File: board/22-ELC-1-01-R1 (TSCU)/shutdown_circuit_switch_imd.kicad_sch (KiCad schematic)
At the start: 9 parts

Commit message: Ready for review
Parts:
- renumbered C1 to C12, D2 to D6, D3 to D7, D4 to D8, D5 to D9, F2 to F1, R1 to R28, R2 to R29, R3 to R30
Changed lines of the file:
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@@
   (symbol (lib_id "Device:R") (at 72.39 137.16 270) (unit 1)
     (in_bom yes) (on_board yes)
-    (property "Reference" "R2" (id 0) (at 72.39 134.62 90))
+    (property "Reference" "R29" (id 0) (at 72.39 134.62 90))
     (property "Value" "10k" (id 1) (at 72.39 137.16 90))
     (property "Footprint" "Resistor_SMD:R_0603_1608Metric_Pad0.98x0.95mm_HandSolder" (id 2) (at 72.39 135.382 90)
@@
   (symbol (lib_id "Device:R") (at 66.04 142.24 180) (unit 1)
     (in_bom yes) (on_board yes)
-    (property "Reference" "R1" (id 0) (at 68.58 142.24 90))
+    (property "Reference" "R28" (id 0) (at 68.58 142.24 90))
     (property "Value" "2.2k" (id 1) (at 66.04 142.24 90))
     (property "Footprint" "Resistor_SMD:R_0603_1608Metric_Pad0.98x0.95mm_HandSolder" (id 2) (at 67.818 142.24 90)
@@
   (symbol (lib_id "power:GND") (at 66.04 146.05 0) (unit 1)
     (in_bom yes) (on_board yes)
-    (property "Reference" "#PWR012" (id 0) (at 66.04 152.4 0)
+    (property "Reference" "#PWR059" (id 0) (at 66.04 152.4 0)
       (effects (font (size 1.27 1.27)) hide)
     )
@@
   (symbol (lib_id "power:GND") (at 90.17 144.78 0) (unit 1)
     (in_bom yes) (on_board yes)
-    (property "Reference" "#PWR016" (id 0) (at 90.17 151.13 0)
+    (property "Reference" "#PWR063" (id 0) (at 90.17 151.13 0)
       (effects (font (size 1.27 1.27)) hide)
     )
@@
   (symbol (lib_id "Device:C_Small") (at 80.01 140.97 180) (unit 1)
     (in_bom yes) (on_board yes)
-    (property "Reference" "C1" (id 0) (at 74.1934 140.97 90))
+    (property "Reference" "C12" (id 0) (at 74.1934 140.97 90))
     (property "Value" "0.1uf" (id 1) (at 76.5048 140.97 90))
     (property "Footprint" "Capacitor_SMD:C_0603_1608Metric_Pad1.08x0.95mm_HandSolder" (id 2) (at 80.01 140.97 0)
@@
   (symbol (lib_id "power:GND") (at 80.01 144.78 0) (unit 1)
     (in_bom yes) (on_board yes)
-    (property "Reference" "#PWR014" (id 0) (at 80.01 151.13 0)
+    (property "Reference" "#PWR061" (id 0) (at 80.01 151.13 0)
       (effects (font (size 1.27 1.27)) hide)
     )
@@
   (symbol (lib_id "Device:R") (at 179.07 144.78 270) (unit 1)
     (in_bom yes) (on_board yes)
-    (property "Reference" "R3" (id 0) (at 179.07 142.24 90))
+    (property "Reference" "R30" (id 0) (at 179.07 142.24 90))
     (property "Value" "1k" (id 1) (at 179.07 144.78 90))
     (property "Footprint" "Resistor_SMD:R_0603_1608Metric_Pad0.98x0.95mm_HandSolder" (id 2) (at 179.07 143.002 90)
@@
   (symbol (lib_id "power:GND") (at 191.77 152.4 0) (unit 1)
     (in_bom yes) (on_board yes)
-    (property "Reference" "#PWR018" (id 0) (at 191.77 158.75 0)
+    (property "Reference" "#PWR065" (id 0) (at 191.77 158.75 0)
       (effects (font (size 1.27 1.27)) hide)
     )
@@
   (symbol (lib_id "Device:Fuse") (at 67.31 82.55 270) (unit 1)
     (in_bom yes) (on_board yes)
-    (property "Reference" "F2" (id 0) (at 67.31 76.2 90))
+    (property "Reference" "F1" (id 0) (at 67.31 76.2 90))
     (property "Value" "2A" (id 1) (at 67.31 78.74 90))
     (property "Footprint" "Fuse:Fuse_1206_3216Metric_Pad1.42x1.75mm_HandSolder" (id 2) (at 67.31 80.772 90)
@@
   (symbol (lib_id "power:+12V") (at 73.66 81.28 0) (unit 1)
     (in_bom yes) (on_board yes)
-    (property "Reference" "#PWR013" (id 0) (at 73.66 85.09 0)
+    (property "Reference" "#PWR060" (id 0) (at 73.66 85.09 0)
       (effects (font (size 1.27 1.27)) hide)
     )
@@
   (symbol (lib_id "power:+5V") (at 90.17 129.54 0) (unit 1)
     (in_bom yes) (on_board yes)
-    (property "Reference" "#PWR015" (id 0) (at 90.17 133.35 0)
+    (property "Reference" "#PWR062" (id 0) (at 90.17 133.35 0)
       (effects (font (size 1.27 1.27)) hide)
     )
@@
   (symbol (lib_id "power:+5V") (at 191.77 137.16 0) (unit 1)
     (in_bom yes) (on_board yes)
-    (property "Reference" "#PWR017" (id 0) (at 191.77 140.97 0)
+    (property "Reference" "#PWR064" (id 0) (at 191.77 140.97 0)
       (effects (font (size 1.27 1.27)) hide)
     )
@@
   (symbol (lib_id "Device:D_Schottky") (at 191.77 148.59 270) (unit 1)
     (in_bom yes) (on_board yes)
-    (property "Reference" "D5" (id 0) (at 193.802 147.4216 90)
+    (property "Reference" "D9" (id 0) (at 193.802 147.4216 90)
       (effects (font (size 1.27 1.27)) (justify left))
     )
@@
   (symbol (lib_id "Device:D_Schottky") (at 191.77 140.97 270) (unit 1)
     (in_bom yes) (on_board yes)
-    (property "Reference" "D4" (id 0) (at 193.802 139.8016 90)
+    (property "Reference" "D8" (id 0) (at 193.802 139.8016 90)
       (effects (font (size 1.27 1.27)) (justify left))
     )
@@
   (symbol (lib_id "Device:D_Schottky") (at 90.17 140.97 270) (unit 1)
     (in_bom yes) (on_board yes)
-    (property "Reference" "D3" (id 0) (at 92.202 139.8016 90)
+    (property "Reference" "D7" (id 0) (at 92.202 139.8016 90)
       (effects (font (size 1.27 1.27)) (justify left))
     )
@@
   (symbol (lib_id "Device:D_Schottky") (at 90.17 133.35 270) (unit 1)
     (in_bom yes) (on_board yes)
-    (property "Reference" "D2" (id 0) (at 92.202 132.1816 90)
-      (effects (font (size 1.27 1.27)) (justify left))
-    )
+    (property "Reference" "D6" (id 0) (at 92.202 132.1816 90)
+      (effects (font (size 1.27 1.27)) (justify left))
+    )

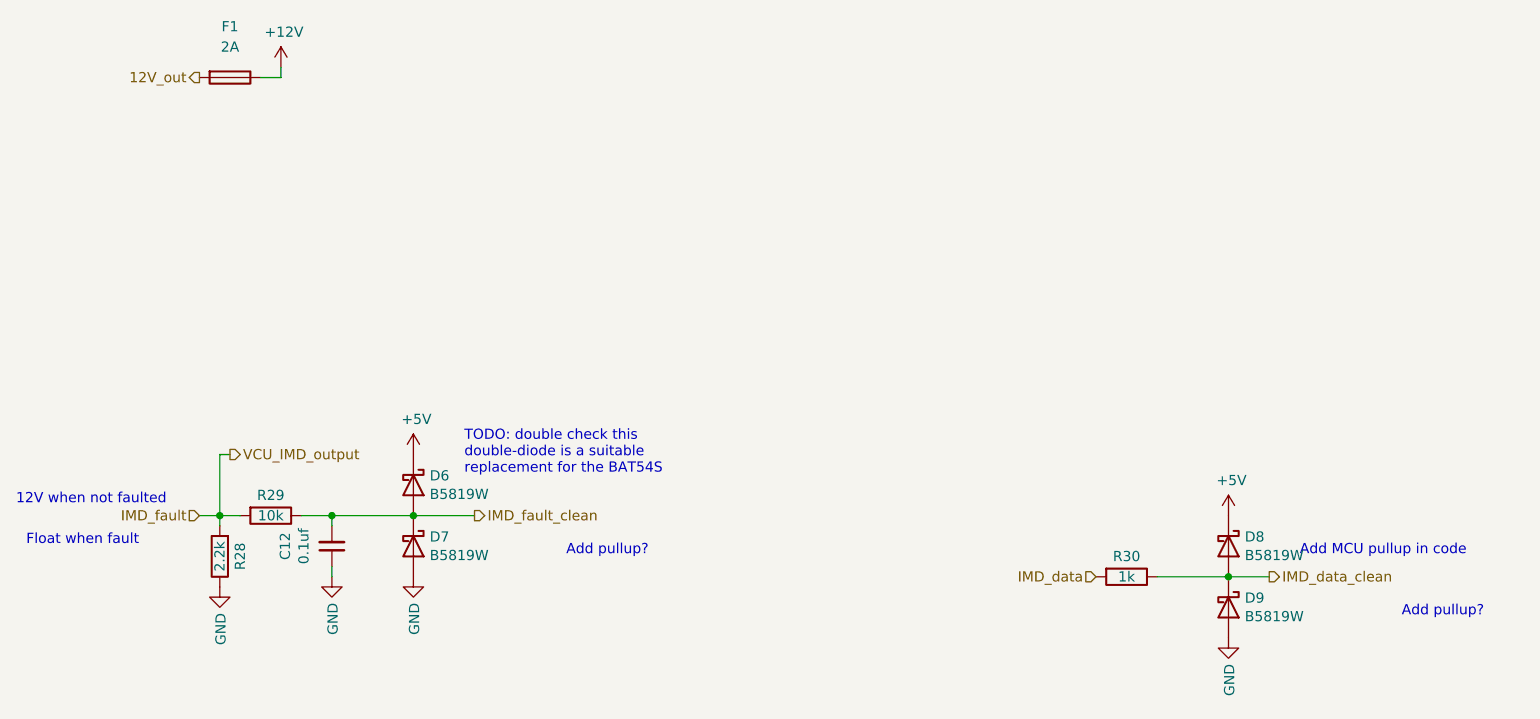
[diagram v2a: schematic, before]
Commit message: All good except need to switch everything to accepting 24v power
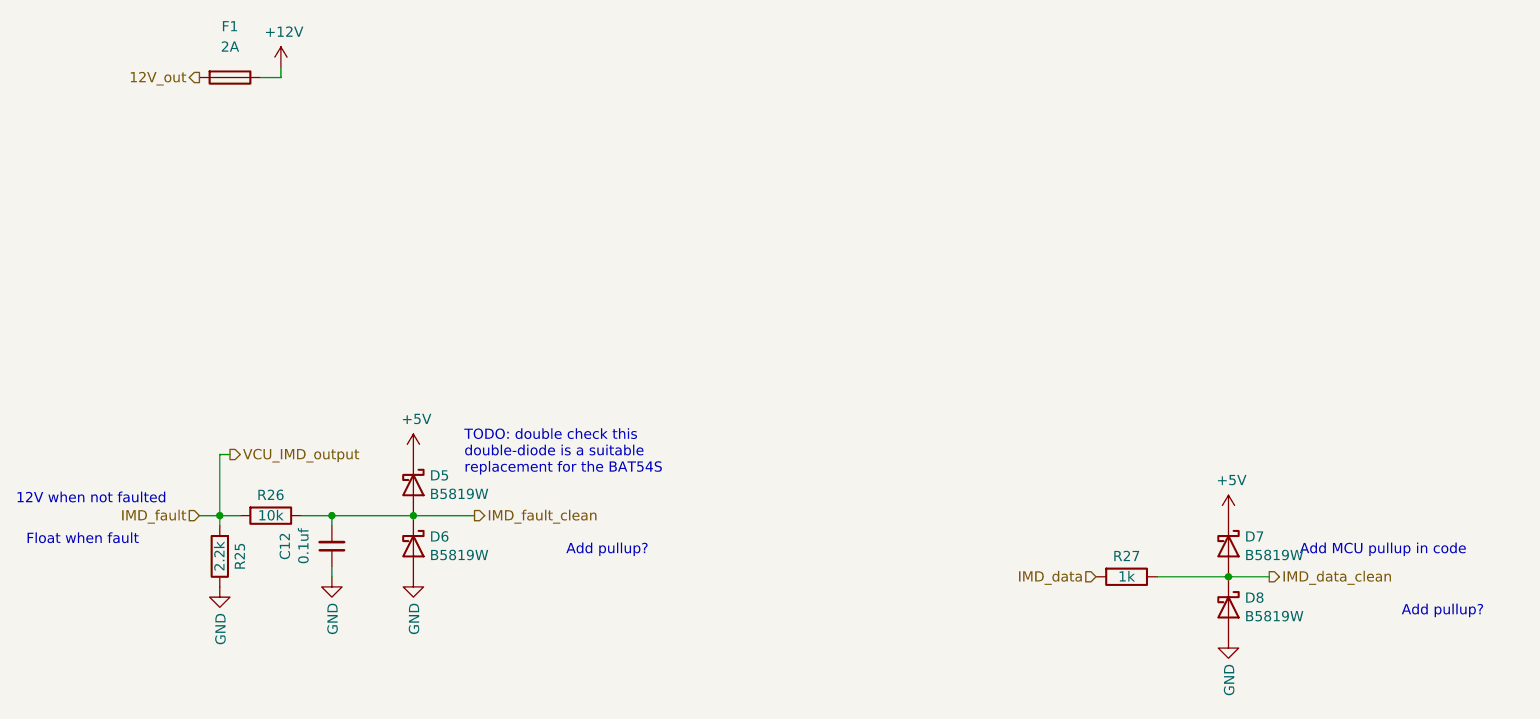
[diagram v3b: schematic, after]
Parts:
- renumbered D6 to D5, D7 to D6, D8 to D7, D9 to D8, R28 to R25, R29 to R26, R30 to R27
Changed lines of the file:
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@@
   (symbol (lib_id "Device:R") (at 72.39 137.16 270) (unit 1)
     (in_bom yes) (on_board yes)
-    (property "Reference" "R29" (id 0) (at 72.39 134.62 90))
+    (property "Reference" "R26" (id 0) (at 72.39 134.62 90))
     (property "Value" "10k" (id 1) (at 72.39 137.16 90))
     (property "Footprint" "Resistor_SMD:R_0603_1608Metric_Pad0.98x0.95mm_HandSolder" (id 2) (at 72.39 135.382 90)
@@
   (symbol (lib_id "Device:R") (at 66.04 142.24 180) (unit 1)
     (in_bom yes) (on_board yes)
-    (property "Reference" "R28" (id 0) (at 68.58 142.24 90))
+    (property "Reference" "R25" (id 0) (at 68.58 142.24 90))
     (property "Value" "2.2k" (id 1) (at 66.04 142.24 90))
     (property "Footprint" "Resistor_SMD:R_0603_1608Metric_Pad0.98x0.95mm_HandSolder" (id 2) (at 67.818 142.24 90)
@@
   (symbol (lib_id "Device:R") (at 179.07 144.78 270) (unit 1)
     (in_bom yes) (on_board yes)
-    (property "Reference" "R30" (id 0) (at 179.07 142.24 90))
+    (property "Reference" "R27" (id 0) (at 179.07 142.24 90))
     (property "Value" "1k" (id 1) (at 179.07 144.78 90))
     (property "Footprint" "Resistor_SMD:R_0603_1608Metric_Pad0.98x0.95mm_HandSolder" (id 2) (at 179.07 143.002 90)
@@
   (symbol (lib_id "Device:D_Schottky") (at 191.77 148.59 270) (unit 1)
     (in_bom yes) (on_board yes)
-    (property "Reference" "D9" (id 0) (at 193.802 147.4216 90)
+    (property "Reference" "D8" (id 0) (at 193.802 147.4216 90)
       (effects (font (size 1.27 1.27)) (justify left))
     )
@@
   (symbol (lib_id "Device:D_Schottky") (at 191.77 140.97 270) (unit 1)
     (in_bom yes) (on_board yes)
-    (property "Reference" "D8" (id 0) (at 193.802 139.8016 90)
+    (property "Reference" "D7" (id 0) (at 193.802 139.8016 90)
       (effects (font (size 1.27 1.27)) (justify left))
     )
@@
   (symbol (lib_id "Device:D_Schottky") (at 90.17 140.97 270) (unit 1)
     (in_bom yes) (on_board yes)
-    (property "Reference" "D7" (id 0) (at 92.202 139.8016 90)
+    (property "Reference" "D6" (id 0) (at 92.202 139.8016 90)
       (effects (font (size 1.27 1.27)) (justify left))
     )
@@
   (symbol (lib_id "Device:D_Schottky") (at 90.17 133.35 270) (unit 1)
     (in_bom yes) (on_board yes)
-    (property "Reference" "D6" (id 0) (at 92.202 132.1816 90)
-      (effects (font (size 1.27 1.27)) (justify left))
-    )
+    (property "Reference" "D5" (id 0) (at 92.202 132.1816 90)
+      (effects (font (size 1.27 1.27)) (justify left))
+    )

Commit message: Finalized schematic, started board layout
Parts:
- C12: footprint Capacitor_SMD:C_0603_1608Metric_Pad1.08x0.95mm_HandSolder -> Capacitor_SMD:C_0402_1005Metric
- R25, R26, R27: footprint Resistor_SMD:R_0603_1608Metric_Pad0.98x0.95mm_HandSolder -> FixedTextSizes:R_0402_1005Metric
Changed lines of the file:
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@@
     (property "Reference" "R26" (id 0) (at 72.39 134.62 90))
     (property "Value" "10k" (id 1) (at 72.39 137.16 90))
-    (property "Footprint" "Resistor_SMD:R_0603_1608Metric_Pad0.98x0.95mm_HandSolder" (id 2) (at 72.39 135.382 90)
+    (property "Footprint" "FixedTextSizes:R_0402_1005Metric" (id 2) (at 72.39 135.382 90)
       (effects (font (size 1.27 1.27)) hide)
     )
@@
     (property "Reference" "R25" (id 0) (at 68.58 142.24 90))
     (property "Value" "2.2k" (id 1) (at 66.04 142.24 90))
-    (property "Footprint" "Resistor_SMD:R_0603_1608Metric_Pad0.98x0.95mm_HandSolder" (id 2) (at 67.818 142.24 90)
+    (property "Footprint" "FixedTextSizes:R_0402_1005Metric" (id 2) (at 67.818 142.24 90)
       (effects (font (size 1.27 1.27)) hide)
     )
@@
   (symbol (lib_id "power:GND") (at 66.04 146.05 0) (unit 1)
     (in_bom yes) (on_board yes)
-    (property "Reference" "#PWR059" (id 0) (at 66.04 152.4 0)
+    (property "Reference" "#PWR058" (id 0) (at 66.04 152.4 0)
       (effects (font (size 1.27 1.27)) hide)
     )
@@
   (symbol (lib_id "power:GND") (at 90.17 144.78 0) (unit 1)
     (in_bom yes) (on_board yes)
-    (property "Reference" "#PWR063" (id 0) (at 90.17 151.13 0)
+    (property "Reference" "#PWR062" (id 0) (at 90.17 151.13 0)
       (effects (font (size 1.27 1.27)) hide)
     )
@@
     (property "Reference" "C12" (id 0) (at 74.1934 140.97 90))
     (property "Value" "0.1uf" (id 1) (at 76.5048 140.97 90))
-    (property "Footprint" "Capacitor_SMD:C_0603_1608Metric_Pad1.08x0.95mm_HandSolder" (id 2) (at 80.01 140.97 0)
+    (property "Footprint" "Capacitor_SMD:C_0402_1005Metric" (id 2) (at 80.01 140.97 0)
       (effects (font (size 1.27 1.27)) hide)
     )
@@
   (symbol (lib_id "power:GND") (at 80.01 144.78 0) (unit 1)
     (in_bom yes) (on_board yes)
-    (property "Reference" "#PWR061" (id 0) (at 80.01 151.13 0)
+    (property "Reference" "#PWR060" (id 0) (at 80.01 151.13 0)
       (effects (font (size 1.27 1.27)) hide)
     )
@@
     (property "Reference" "R27" (id 0) (at 179.07 142.24 90))
     (property "Value" "1k" (id 1) (at 179.07 144.78 90))
-    (property "Footprint" "Resistor_SMD:R_0603_1608Metric_Pad0.98x0.95mm_HandSolder" (id 2) (at 179.07 143.002 90)
+    (property "Footprint" "FixedTextSizes:R_0402_1005Metric" (id 2) (at 179.07 143.002 90)
       (effects (font (size 1.27 1.27)) hide)
     )
@@
   (symbol (lib_id "power:GND") (at 191.77 152.4 0) (unit 1)
     (in_bom yes) (on_board yes)
-    (property "Reference" "#PWR065" (id 0) (at 191.77 158.75 0)
+    (property "Reference" "#PWR064" (id 0) (at 191.77 158.75 0)
       (effects (font (size 1.27 1.27)) hide)
     )
@@
   (symbol (lib_id "power:+12V") (at 73.66 81.28 0) (unit 1)
     (in_bom yes) (on_board yes)
-    (property "Reference" "#PWR060" (id 0) (at 73.66 85.09 0)
+    (property "Reference" "#PWR059" (id 0) (at 73.66 85.09 0)
       (effects (font (size 1.27 1.27)) hide)
     )
@@
   (symbol (lib_id "power:+5V") (at 90.17 129.54 0) (unit 1)
     (in_bom yes) (on_board yes)
-    (property "Reference" "#PWR062" (id 0) (at 90.17 133.35 0)
+    (property "Reference" "#PWR061" (id 0) (at 90.17 133.35 0)
       (effects (font (size 1.27 1.27)) hide)
     )
@@
   (symbol (lib_id "power:+5V") (at 191.77 137.16 0) (unit 1)
     (in_bom yes) (on_board yes)
-    (property "Reference" "#PWR064" (id 0) (at 191.77 140.97 0)
-      (effects (font (size 1.27 1.27)) hide)
-    )
+    (property "Reference" "#PWR063" (id 0) (at 191.77 140.97 0)
+      (effects (font (size 1.27 1.27)) hide)
+    )

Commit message: More progress
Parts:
- C12: footprint Capacitor_SMD:C_0402_1005Metric -> FixedTextSizes:C_0402_1005Metric_Pad0.74x0.62mm_HandSolder_Reasonable_Text_Size
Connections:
- net +12V renamed +24V
- net 12V_out renamed 24V_out
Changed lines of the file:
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@@
     (effects (font (size 1.27 1.27)) (justify left))
   )
-  (hierarchical_label "12V_out" (shape output) (at 63.5 82.55 180)
+  (hierarchical_label "24V_out" (shape output) (at 63.5 82.55 180)
     (effects (font (size 1.27 1.27)) (justify right))
   )
@@
   (symbol (lib_id "power:GND") (at 66.04 146.05 0) (unit 1)
     (in_bom yes) (on_board yes)
-    (property "Reference" "#PWR058" (id 0) (at 66.04 152.4 0)
+    (property "Reference" "#PWR061" (id 0) (at 66.04 152.4 0)
       (effects (font (size 1.27 1.27)) hide)
     )
@@
   (symbol (lib_id "power:GND") (at 90.17 144.78 0) (unit 1)
     (in_bom yes) (on_board yes)
-    (property "Reference" "#PWR062" (id 0) (at 90.17 151.13 0)
+    (property "Reference" "#PWR065" (id 0) (at 90.17 151.13 0)
       (effects (font (size 1.27 1.27)) hide)
     )
@@
     (property "Reference" "C12" (id 0) (at 74.1934 140.97 90))
     (property "Value" "0.1uf" (id 1) (at 76.5048 140.97 90))
-    (property "Footprint" "Capacitor_SMD:C_0402_1005Metric" (id 2) (at 80.01 140.97 0)
+    (property "Footprint" "FixedTextSizes:C_0402_1005Metric_Pad0.74x0.62mm_HandSolder_Reasonable_Text_Size" (id 2) (at 80.01 140.97 0)
       (effects (font (size 1.27 1.27)) hide)
     )
@@
   (symbol (lib_id "power:GND") (at 80.01 144.78 0) (unit 1)
     (in_bom yes) (on_board yes)
-    (property "Reference" "#PWR060" (id 0) (at 80.01 151.13 0)
+    (property "Reference" "#PWR063" (id 0) (at 80.01 151.13 0)
       (effects (font (size 1.27 1.27)) hide)
     )
@@
   (symbol (lib_id "power:GND") (at 191.77 152.4 0) (unit 1)
     (in_bom yes) (on_board yes)
-    (property "Reference" "#PWR064" (id 0) (at 191.77 158.75 0)
+    (property "Reference" "#PWR067" (id 0) (at 191.77 158.75 0)
       (effects (font (size 1.27 1.27)) hide)
     )
@@
     (pin "2")
   )
-  (symbol (lib_id "power:+12V") (at 73.66 81.28 0) (unit 1)
-    (in_bom yes) (on_board yes)
-    (property "Reference" "#PWR059" (id 0) (at 73.66 85.09 0)
-      (effects (font (size 1.27 1.27)) hide)
-    )
-    (property "Value" "+12V" (id 1) (at 74.041 76.8858 0))
-    (property "Footprint" "" (id 2) (at 73.66 81.28 0)
-      (effects (font (size 1.27 1.27)) hide)
-    )
-    (property "Datasheet" "" (id 3) (at 73.66 81.28 0)
-      (effects (font (size 1.27 1.27)) hide)
-    )
-    (pin "1")
-  )
   (symbol (lib_id "power:+5V") (at 90.17 129.54 0) (unit 1)
     (in_bom yes) (on_board yes)
-    (property "Reference" "#PWR061" (id 0) (at 90.17 133.35 0)
+    (property "Reference" "#PWR064" (id 0) (at 90.17 133.35 0)
       (effects (font (size 1.27 1.27)) hide)
     )
@@
   (symbol (lib_id "power:+5V") (at 191.77 137.16 0) (unit 1)
     (in_bom yes) (on_board yes)
-    (property "Reference" "#PWR063" (id 0) (at 191.77 140.97 0)
+    (property "Reference" "#PWR066" (id 0) (at 191.77 140.97 0)
       (effects (font (size 1.27 1.27)) hide)
     )
@@
     (pin "2")
   )
+  (symbol (lib_id "power:+24V") (at 73.66 81.28 0) (unit 1)
+    (in_bom yes) (on_board yes) (fields_autoplaced)
+    (property "Reference" "#PWR062" (id 0) (at 73.66 85.09 0)
+      (effects (font (size 1.27 1.27)) hide)
+    )
+    (property "Value" "+24V" (id 1) (at 73.66 76.2 0))
+    (property "Footprint" "" (id 2) (at 73.66 81.28 0)
+      (effects (font (size 1.27 1.27)) hide)
+    )
+    (property "Datasheet" "" (id 3) (at 73.66 81.28 0)
+      (effects (font (size 1.27 1.27)) hide)
+    )
+    (pin "1")
+  )
 )
